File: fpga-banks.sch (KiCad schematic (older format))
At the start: 14 parts, among them U1 XC7K70T-FBG484, U2 ASEM1-100.000MHZ-LC-T

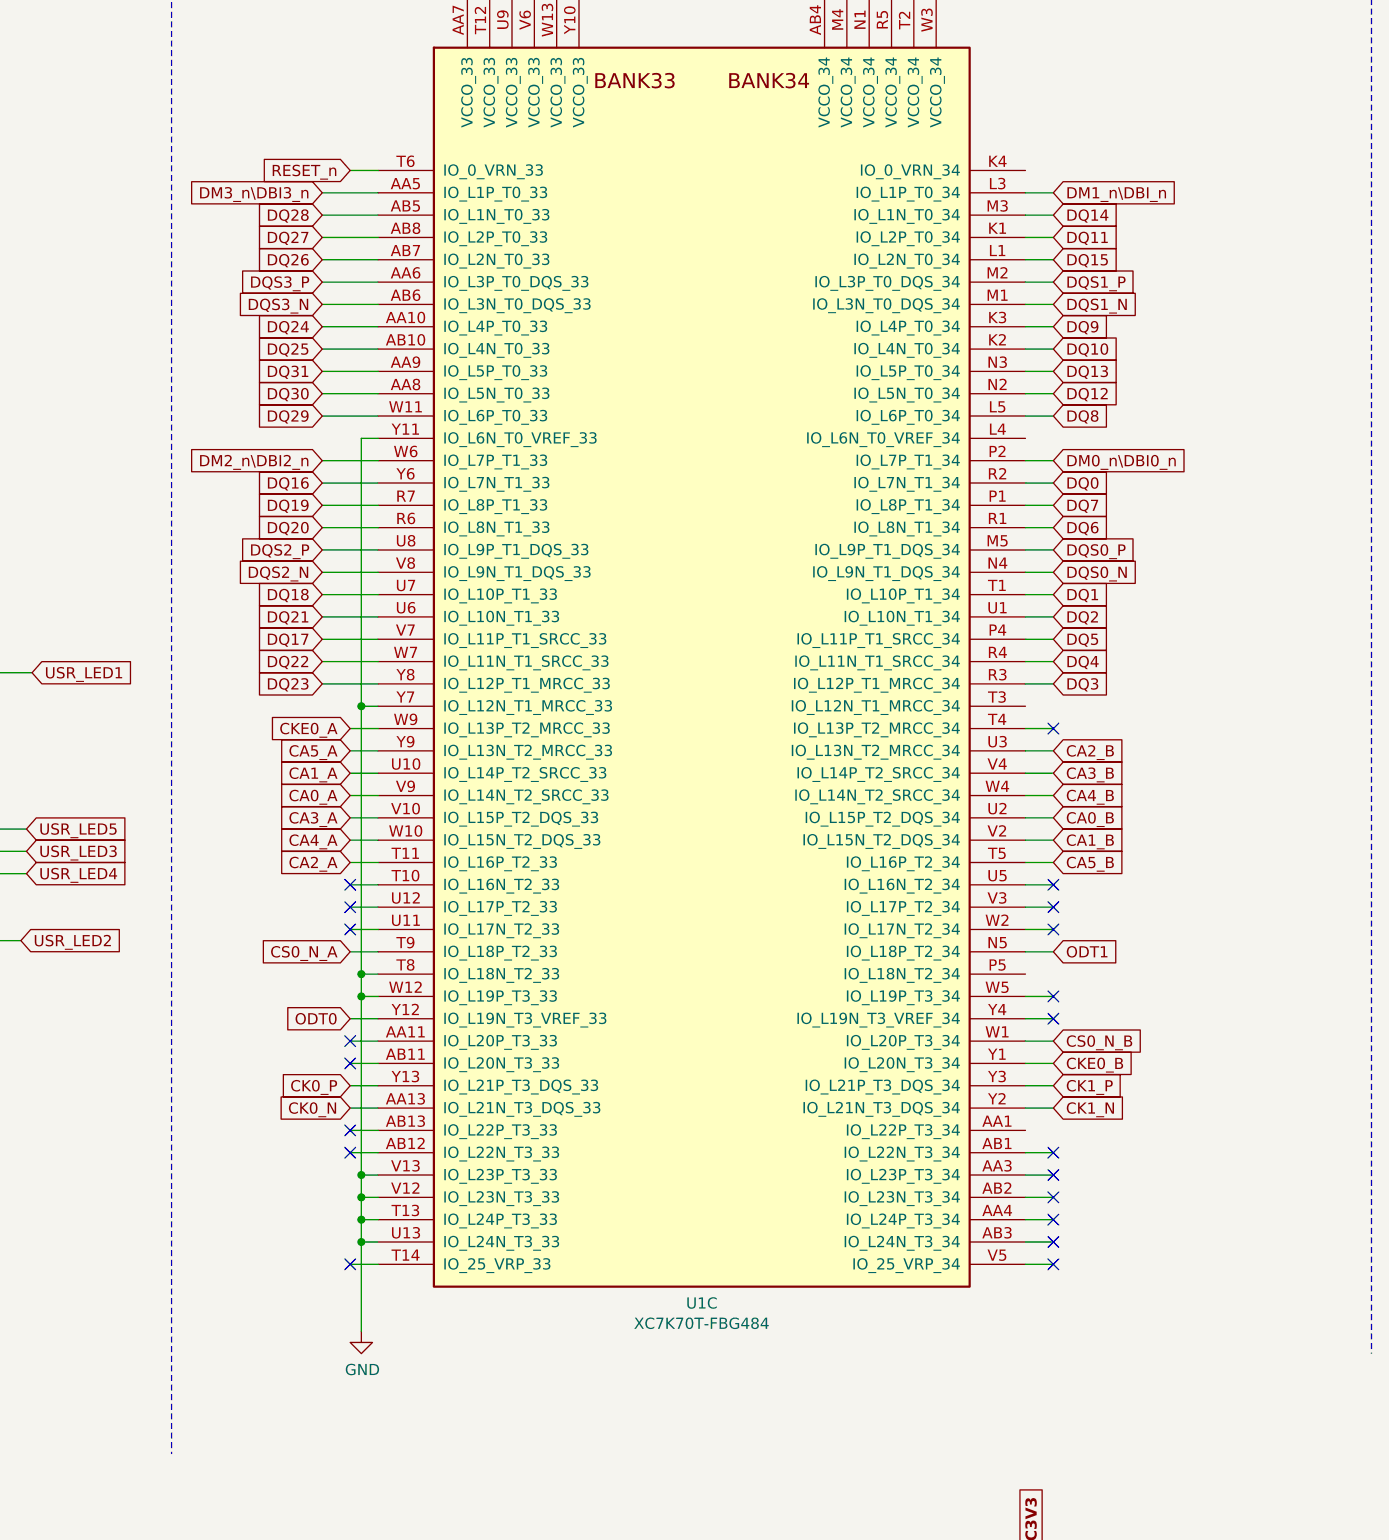
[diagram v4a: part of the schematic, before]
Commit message: re-assinged DDR4 Channel A DQ and CA lanes
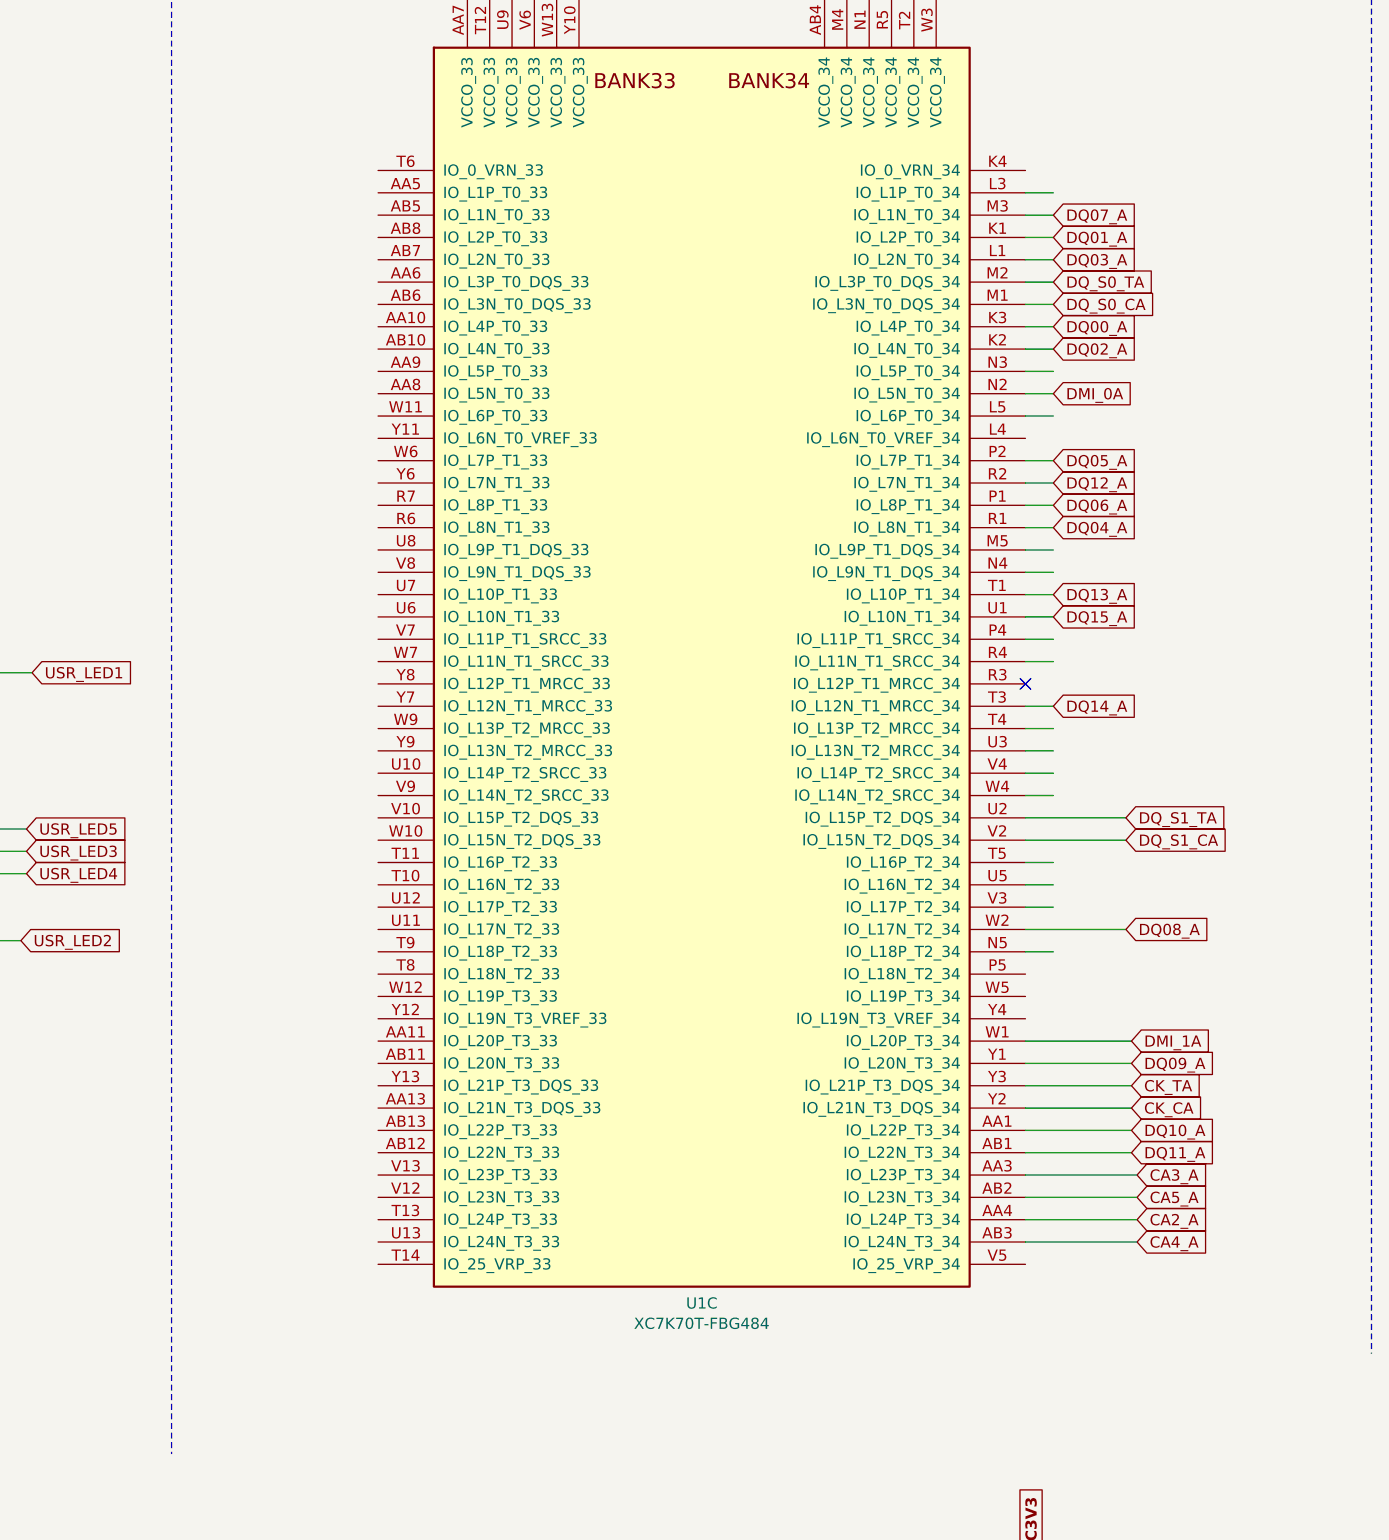
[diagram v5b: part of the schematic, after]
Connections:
- net labels added: CK_CA, CK_TA, DMI_0A, DMI_1A, DQ00_A, DQ01_A, DQ02_A, DQ03_A, DQ04_A, DQ05_A, DQ06_A, DQ07_A, DQ08_A, DQ09_A, DQ10_A, DQ11_A, DQ12_A, DQ13_A, DQ14_A, DQ15_A, DQ_S0_CA, DQ_S0_TA, DQ_S1_CA, DQ_S1_TA
- net labels removed: CA0_A, CA0_B, CA1_A, CA1_B, CA2_B, CA3_B, CA4_B, CA5_B, CK0_N, CK0_P, CK1_N, CK1_P, CKE0_A, CKE0_B, CS0_N_A, CS0_N_B, DM0_n\DBI0_n, DM1_n\DBI_n, DM2_n\DBI2_n, DM3_n\DBI3_n, DQ0, DQ1, DQ10, DQ11, DQ12, DQ13, DQ14, DQ15, DQ16, DQ17, DQ18, DQ19, DQ2, DQ20, DQ21, DQ22, DQ23, DQ24, DQ25, DQ26, DQ27, DQ28, DQ29, DQ3, DQ30, DQ31, DQ4, DQ5, DQ6, DQ7, DQ8, DQ9, DQS0_N, DQS0_P, DQS1_N, DQS1_P, DQS2_N, DQS2_P, DQS3_N, DQS3_P, ODT0, ODT1, RESET_n
- wire segments 262 -> 202
- no-connect marks 59 -> 40

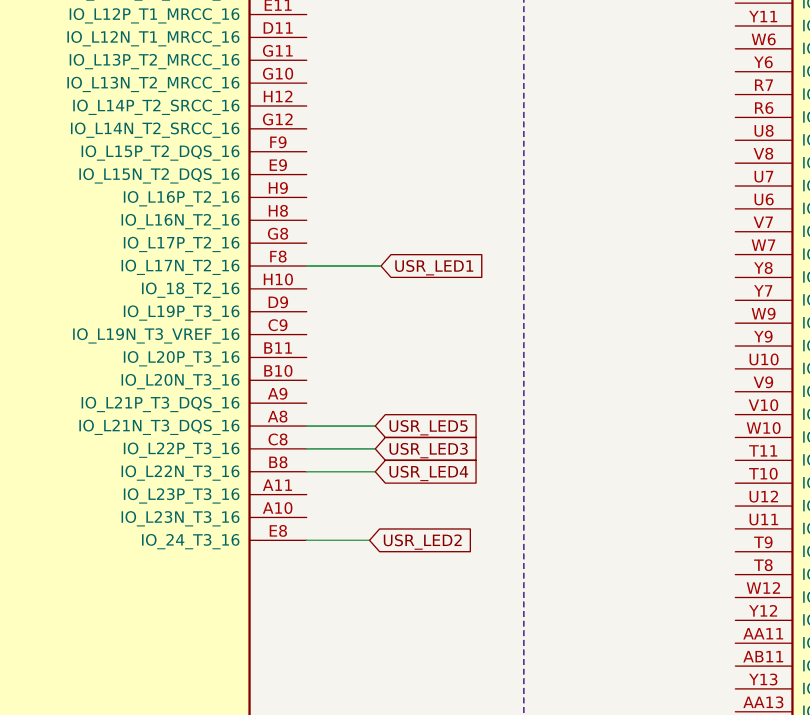
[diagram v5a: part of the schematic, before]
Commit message: Add User buttons to schematic
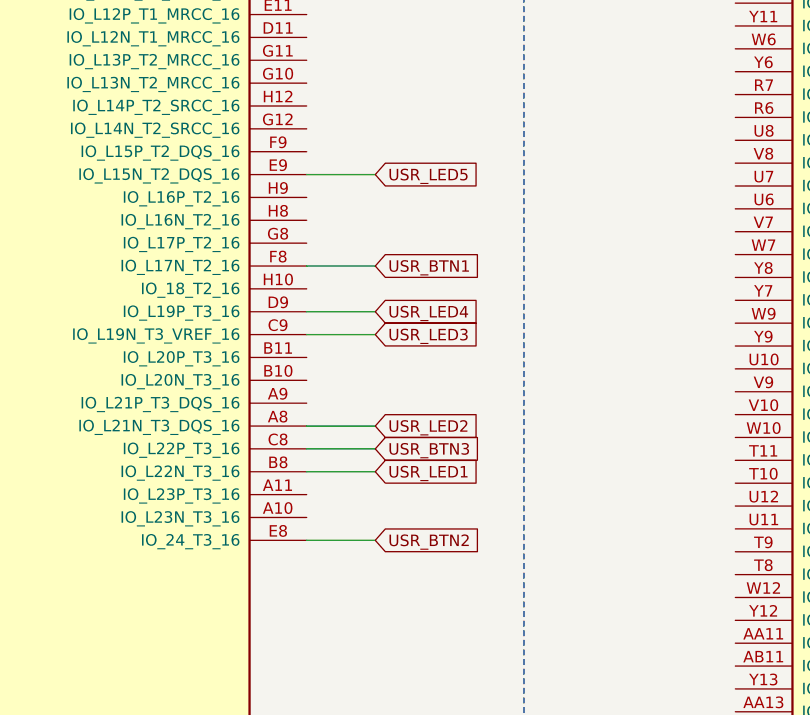
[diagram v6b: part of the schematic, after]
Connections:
- net labels added: USR_BTN1, USR_BTN2, USR_BTN3
- wire segments 202 -> 205
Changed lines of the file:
@@
 Text Notes 5950 2950 1    50   ~ 0
 config-spi.sch
-Text GLabel 10550 4475 2    50   Input ~ 0
+Text GLabel 10525 5375 2    50   Input ~ 0
 USR_LED1
-Text GLabel 10500 5675 2    50   Input ~ 0
+Text GLabel 10525 5175 2    50   Input ~ 0
 USR_LED2
-Text GLabel 10525 5275 2    50   Input ~ 0
+Text GLabel 10525 4775 2    50   Input ~ 0
 USR_LED3
-Text GLabel 10525 5375 2    50   Input ~ 0
-USR_LED4
-Text GLabel 10525 5175 2    50   Input ~ 0
+Text GLabel 10525 4075 2    50   Input ~ 0
 USR_LED5
 Wire Wire Line
@@
 CSI_B used for config
 Wire Wire Line
-	10550 4475 10225 4475
-Wire Wire Line
-	10225 5675 10500 5675
+	10525 5375 10225 5375
 Wire Wire Line
 	10225 5175 10525 5175
 Wire Wire Line
-	10225 5275 10525 5275
-Wire Wire Line
-	10225 5375 10525 5375
+	10225 4075 10525 4075
+Wire Wire Line
+	10225 4775 10525 4775
 Wire Wire Line
 	4800 3400 5300 3400
@@
 Text GLabel 15500 6925 2    50   Input ~ 0
 CA2_A
+Text GLabel 10525 4475 2    50   Input ~ 0
+USR_BTN1
+Text GLabel 10525 5675 2    50   Input ~ 0
+USR_BTN2
+Text GLabel 10525 5275 2    50   Input ~ 0
+USR_BTN3
+Wire Wire Line
+	10225 4475 10525 4475
+Wire Wire Line
+	10225 5675 10525 5675
+Wire Wire Line
+	10225 5275 10525 5275
+Wire Wire Line
+	10225 4675 10525 4675
+Text GLabel 10525 4675 2    50   Input ~ 0
+USR_LED4
 $EndSCHEMATC

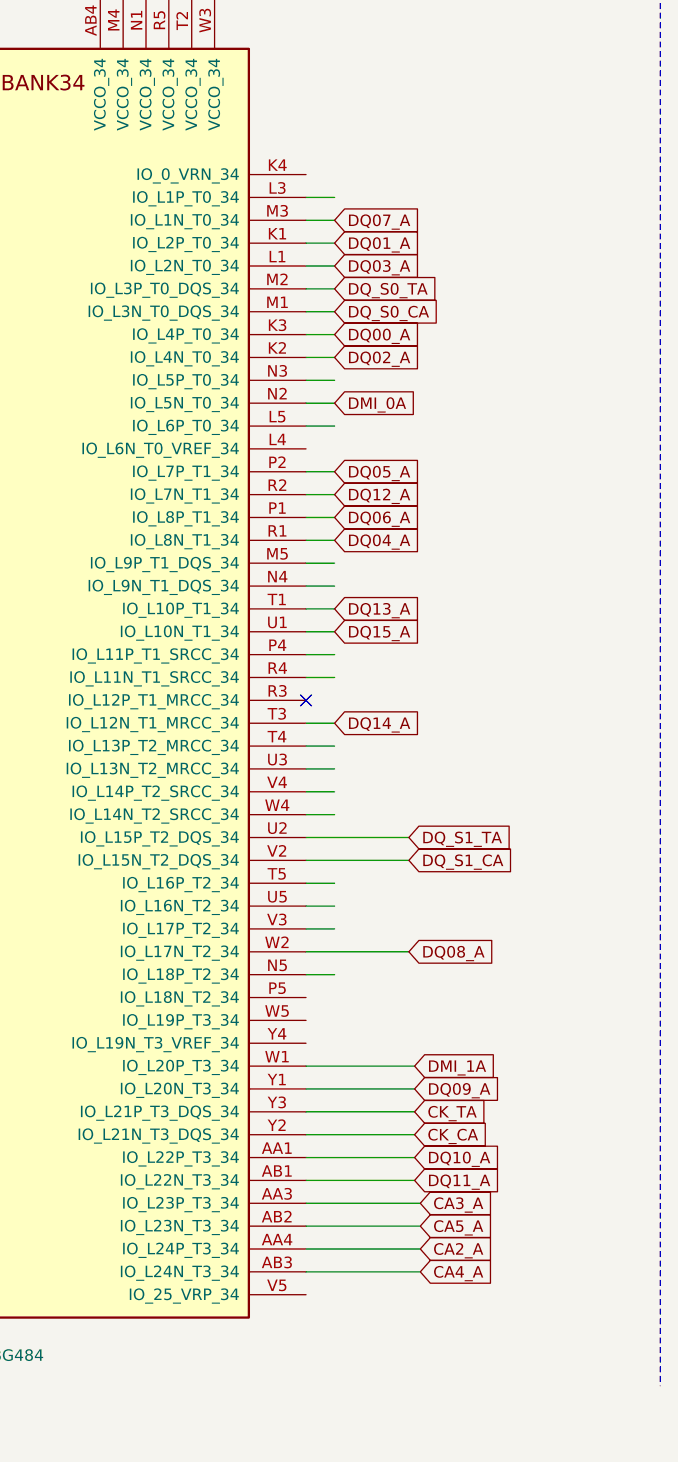
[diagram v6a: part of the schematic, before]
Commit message: Connect CA and spare IOs to SODIMM
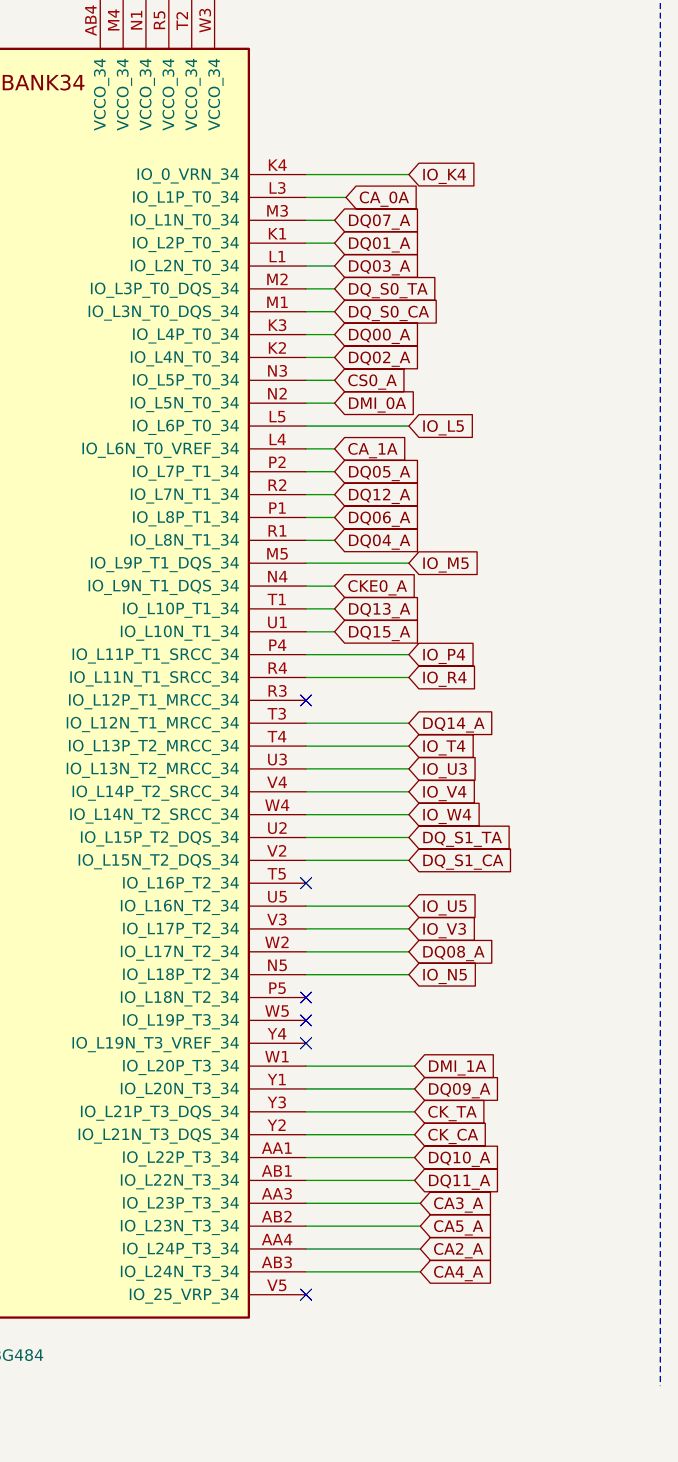
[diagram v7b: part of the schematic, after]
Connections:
- net labels added: CA_0A, CA_1A, CKE0_A, CS0_A, IO_K4, IO_L5, IO_M5, IO_N5, IO_P4, IO_R4, IO_T4, IO_U3, IO_U5, IO_V3, IO_V4, IO_W4
- wire segments 205 -> 206
- no-connect marks 40 -> 45
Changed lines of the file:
@@
 $EndComp
 Wire Wire Line
-	15000 4725 15125 4725
-Wire Wire Line
-	15000 4825 15125 4825
-Wire Wire Line
-	15000 4925 15125 4925
-Wire Wire Line
-	15000 5025 15125 5025
+	15000 4825 15450 4825
+Wire Wire Line
+	15000 4925 15450 4925
 Wire Wire Line
 	15000 5125 15450 5125
@@
 	15000 5225 15450 5225
 Wire Wire Line
-	15000 5325 15125 5325
-Wire Wire Line
-	15000 5425 15125 5425
-Wire Wire Line
-	15000 5525 15125 5525
-Wire Wire Line
-	15000 5725 15125 5725
+	15000 5425 15450 5425
+Wire Wire Line
+	15000 5525 15450 5525
+Wire Wire Line
+	15000 5725 15450 5725
 Text Notes 11475 1000 0    98   ~ 20
 LPDDR4-TESTBED
@@
 NoConn ~ 1900 5300
 Wire Wire Line
-	15125 4425 15000 4425
-Wire Wire Line
-	15125 4325 15000 4325
+	15450 4325 15000 4325
 Wire Wire Line
 	15125 4225 15000 4225
@@
 	15125 4025 15000 4025
 Wire Wire Line
-	15125 3925 15000 3925
+	15450 3925 15000 3925
 Wire Wire Line
 	15125 3825 15000 3825
@@
 	15125 3525 15000 3525
 Wire Wire Line
-	15125 2325 15000 2325
+	15175 2325 15000 2325
 Wire Wire Line
 	15125 2425 15000 2425
@@
 	15125 3225 15000 3225
 Wire Wire Line
-	15125 3325 15000 3325
+	15450 3325 15000 3325
 Wire Wire Line
 	7725 1475 7725 1350
@@
 Text GLabel 15125 4225 2    50   Input ~ 0
 DQ15_A
-Text GLabel 15125 4625 2    50   Input ~ 0
+Text GLabel 15450 4625 2    50   Input ~ 0
 DQ14_A
 Text GLabel 15125 4125 2    50   Input ~ 0
@@
 	15500 6725 15000 6725
 Wire Wire Line
-	15000 4625 15125 4625
+	15000 4625 15450 4625
 NoConn ~ 15000 4525
 Wire Wire Line
@@
 Text GLabel 10525 4675 2    50   Input ~ 0
 USR_LED4
+Text GLabel 15175 2325 2    50   Input ~ 0
+CA_0A
+Text GLabel 15125 3425 2    50   Input ~ 0
+CA_1A
+Wire Wire Line
+	15000 2225 15450 2225
+Text GLabel 15125 3125 2    50   Input ~ 0
+CS0_A
+Text GLabel 15125 4025 2    50   Input ~ 0
+CKE0_A
+Wire Wire Line
+	15000 3425 15125 3425
+Text GLabel 15450 5025 2    50   Input ~ 0
+IO_W4
+Wire Wire Line
+	15000 5025 15450 5025
+Text GLabel 15450 4925 2    50   Input ~ 0
+IO_V4
+Text GLabel 15450 5525 2    50   Input ~ 0
+IO_V3
+Text GLabel 15450 4825 2    50   Input ~ 0
+IO_U3
+Text GLabel 15450 4725 2    50   Input ~ 0
+IO_T4
+Wire Wire Line
+	15000 4725 15450 4725
+Text GLabel 15450 4425 2    50   Input ~ 0
+IO_R4
+Wire Wire Line
+	15000 4425 15450 4425
+Text GLabel 15450 4325 2    50   Input ~ 0
+IO_P4
+Text GLabel 15450 3925 2    50   Input ~ 0
+IO_M5
+Text GLabel 15450 3325 2    50   Input ~ 0
+IO_L5
+Text GLabel 15450 2225 2    50   Input ~ 0
+IO_K4
+NoConn ~ 15000 5325
+Text GLabel 15450 5425 2    50   Input ~ 0
+IO_U5
+NoConn ~ 15000 5925
+NoConn ~ 15000 5825
+Text GLabel 15450 5725 2    50   Input ~ 0
+IO_N5
+NoConn ~ 15000 6025
+NoConn ~ 15000 7125
 $EndSCHEMATC
